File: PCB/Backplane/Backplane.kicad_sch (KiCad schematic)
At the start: 0 parts

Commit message: Backplane connectors
Got the labeling on the connectors done, just the connecting needs to be done
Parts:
- added J1, J10, J2, J3, J4, J5, J6, J7, J8, J9: 5530843-7, 5530843-7:TE_5530843-7, symbol 5530843-7:5530843-7
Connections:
- new net 1: J1.1, J10.1, J2.1, J3.1, J4.1, J5.1, J6.1, J7.1, J8.1, J9.1
- new net 10: J1.10, J10.10, J2.10, J3.10, J4.10, J5.10, J6.10, J7.10, J8.10, J9.10
- new net 11: J1.11, J10.11, J2.11, J3.11, J4.11, J5.11, J6.11, J7.11, J8.11, J9.11
- new net 12: J1.12, J10.12, J2.12, J3.12, J4.12, J5.12, J6.12, J7.12, J8.12, J9.12
- new net 13: J1.13, J10.13, J2.13, J3.13, J4.13, J5.13, J6.13, J7.13, J8.13, J9.13
- new net 14: J1.14, J10.14, J2.14, J3.14, J4.14, J5.14, J6.14, J7.14, J8.14, J9.14
- new net 15: J1.15, J10.15, J2.15, J3.15, J4.15, J5.15, J6.15, J7.15, J8.15, J9.15
- new net 16: J1.16, J10.16, J2.16, J3.16, J4.16, J5.16, J6.16, J7.16, J8.16, J9.16
- new net 17: J1.17, J10.17, J2.17, J3.17, J4.17, J5.17, J6.17, J7.17, J8.17, J9.17
- new net 18: J1.18, J10.18, J2.18, J3.18, J4.18, J5.18, J6.18, J7.18, J8.18, J9.18
- new net 19: J1.19, J10.19, J2.19, J3.19, J4.19, J5.19, J6.19, J7.19, J8.19, J9.19
- new net 2: J1.2, J10.2, J2.2, J3.2, J4.2, J5.2, J6.2, J7.2, J8.2, J9.2
- new net 20: J1.20, J10.20, J2.20, J3.20, J4.20, J5.20, J6.20, J7.20, J8.20, J9.20
- new net 21: J1.21, J10.21, J2.21, J3.21, J4.21, J5.21, J6.21, J7.21, J8.21, J9.21
- new net 22: J1.22, J10.22, J2.22, J3.22, J4.22, J5.22, J6.22, J7.22, J8.22, J9.22
- new net 23: J1.23, J10.23, J2.23, J3.23, J4.23, J5.23, J6.23, J7.23, J8.23, J9.23
- new net 24: J1.24, J10.24, J2.24, J3.24, J4.24, J5.24, J6.24, J7.24, J8.24, J9.24
- new net 25: J1.25, J10.25, J2.25, J3.25, J4.25, J5.25, J6.25, J7.25, J8.25, J9.25
- new net 26: J1.26, J10.26, J2.26, J3.26, J4.26, J5.26, J6.26, J7.26, J8.26, J9.26
- new net 27: J1.27, J10.27, J2.27, J3.27, J4.27, J5.27, J6.27, J7.27, J8.27, J9.27
- new net 28: J1.28, J10.28, J2.28, J3.28, J4.28, J5.28, J6.28, J7.28, J8.28, J9.28
- new net 29: J1.29, J10.29, J2.29, J3.29, J4.29, J5.29, J6.29, J7.29, J8.29, J9.29
- new net 3: J1.3, J10.3, J2.3, J3.3, J4.3, J5.3, J6.3, J7.3, J8.3, J9.3
- new net 30: J1.30, J10.30, J2.30, J3.30, J4.30, J5.30, J6.30, J7.30, J8.30, J9.30
- new net 31: J1.31, J10.31, J2.31, J3.31, J4.31, J5.31, J6.31, J7.31, J8.31, J9.31
- new net 32: J1.32, J10.32, J2.32, J3.32, J4.32, J5.32, J6.32, J7.32, J8.32, J9.32
- new net 33: J1.33, J10.33, J2.33, J3.33, J4.33, J5.33, J6.33, J7.33, J8.33, J9.33
- new net 34: J1.34, J10.34, J2.34, J3.34, J4.34, J5.34, J6.34, J7.34, J8.34, J9.34
- new net 35: J1.35, J10.35, J2.35, J3.35, J4.35, J5.35, J6.35, J7.35, J8.35, J9.35
- new net 36: J1.36, J10.36, J2.36, J3.36, J4.36, J5.36, J6.36, J7.36, J8.36, J9.36
- new net 37: J1.37, J10.37, J2.37, J3.37, J4.37, J5.37, J6.37, J7.37, J8.37, J9.37
- new net 38: J1.38, J10.38, J2.38, J3.38, J4.38, J5.38, J6.38, J7.38, J8.38, J9.38
- new net 39: J1.39, J10.39, J2.39, J3.39, J4.39, J5.39, J6.39, J7.39, J8.39, J9.39
- new net 4: J1.4, J10.4, J2.4, J3.4, J4.4, J5.4, J6.4, J7.4, J8.4, J9.4
- new net 40: J1.40, J10.40, J2.40, J3.40, J4.40, J5.40, J6.40, J7.40, J8.40, J9.40
- new net 41: J1.41, J10.41, J2.41, J3.41, J4.41, J5.41, J6.41, J7.41, J8.41, J9.41
- new net 42: J1.42, J10.42, J2.42, J3.42, J4.42, J5.42, J6.42, J7.42, J8.42, J9.42
- new net 43: J1.43, J10.43, J2.43, J3.43, J4.43, J5.43, J6.43, J7.43, J8.43, J9.43
- new net 44: J1.44, J10.44, J2.44, J3.44, J4.44, J5.44, J6.44, J7.44, J8.44, J9.44
- new net 45: J1.45, J10.45, J2.45, J3.45, J4.45, J5.45, J6.45, J7.45, J8.45, J9.45
- new net 46: J1.46, J10.46, J2.46, J3.46, J4.46, J5.46, J6.46, J7.46, J8.46, J9.46
- new net 47: J1.47, J10.47, J2.47, J3.47, J4.47, J5.47, J6.47, J7.47, J8.47, J9.47
- new net 48: J1.48, J10.48, J2.48, J3.48, J4.48, J5.48, J6.48, J7.48, J8.48, J9.48
- new net 49: J1.49, J10.49, J2.49, J3.49, J4.49, J5.49, J6.49, J7.49, J8.49, J9.49
- new net 5: J1.5, J10.5, J2.5, J3.5, J4.5, J5.5, J6.5, J7.5, J8.5, J9.5
- new net 50: J1.50, J10.50, J2.50, J3.50, J4.50, J5.50, J6.50, J7.50, J8.50, J9.50
- new net 51: J1.51, J10.51, J2.51, J3.51, J4.51, J5.51, J6.51, J7.51, J8.51, J9.51
- new net 52: J1.52, J10.52, J2.52, J3.52, J4.52, J5.52, J6.52, J7.52, J8.52, J9.52
- new net 53: J1.53, J10.53, J2.53, J3.53, J4.53, J5.53, J6.53, J7.53, J8.53, J9.53
- new net 54: J1.54, J10.54, J2.54, J3.54, J4.54, J5.54, J6.54, J7.54, J8.54, J9.54
- new net 55: J1.55, J10.55, J2.55, J3.55, J4.55, J5.55, J6.55, J7.55, J8.55, J9.55
- new net 56: J1.56, J10.56, J2.56, J3.56, J4.56, J5.56, J6.56, J7.56, J8.56, J9.56
- new net 57: J1.57, J10.57, J2.57, J3.57, J4.57, J5.57, J6.57, J7.57, J8.57, J9.57
- new net 58: J1.58, J10.58, J2.58, J3.58, J4.58, J5.58, J6.58, J7.58, J8.58, J9.58
- new net 59: J1.59, J10.59, J2.59, J3.59, J4.59, J5.59, J6.59, J7.59, J8.59, J9.59
- new net 6: J1.6, J10.6, J2.6, J3.6, J4.6, J5.6, J6.6, J7.6, J8.6, J9.6
- new net 60: J1.60, J10.60, J2.60, J3.60, J4.60, J5.60, J6.60, J7.60, J8.60, J9.60
- new net 7: J1.7, J10.7, J2.7, J3.7, J4.7, J5.7, J6.7, J7.7, J8.7, J9.7
- new net 8: J1.8, J10.8, J2.8, J3.8, J4.8, J5.8, J6.8, J7.8, J8.8, J9.8
- new net 9: J1.9, J10.9, J2.9, J3.9, J4.9, J5.9, J6.9, J7.9, J8.9, J9.9

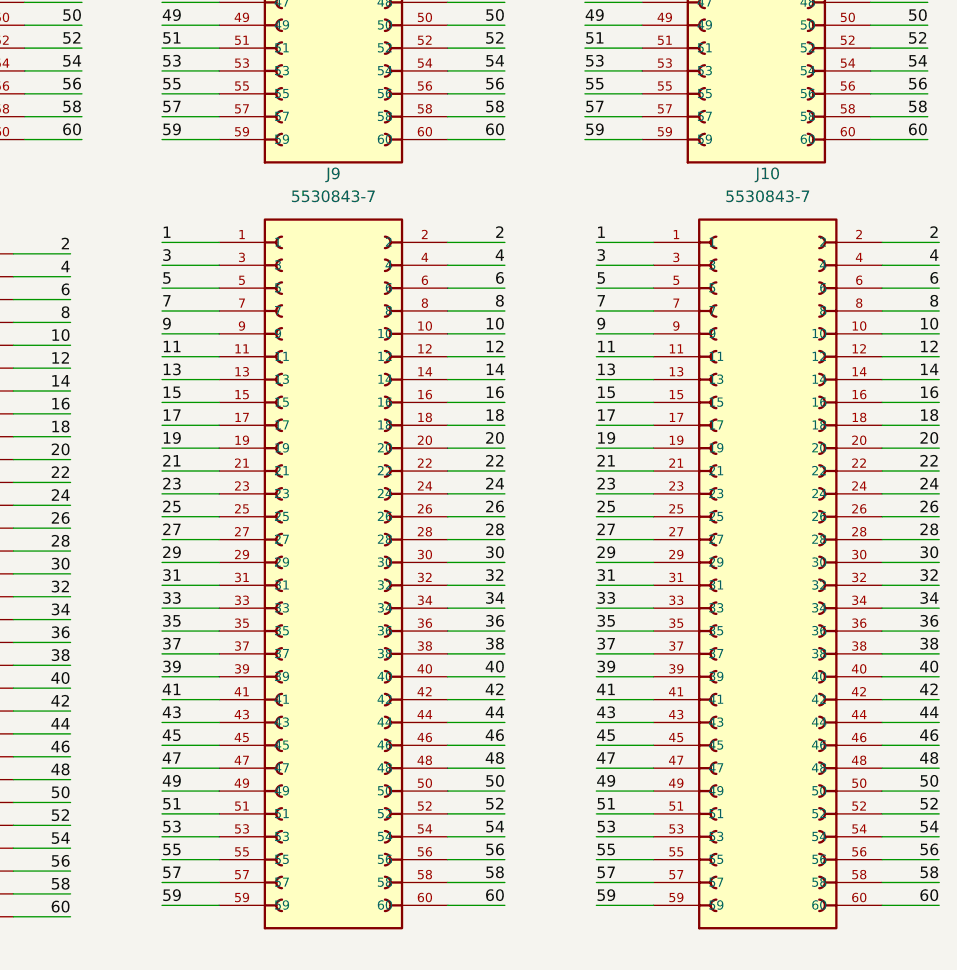
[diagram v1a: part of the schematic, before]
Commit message: Updated backplane and removed unused connectors
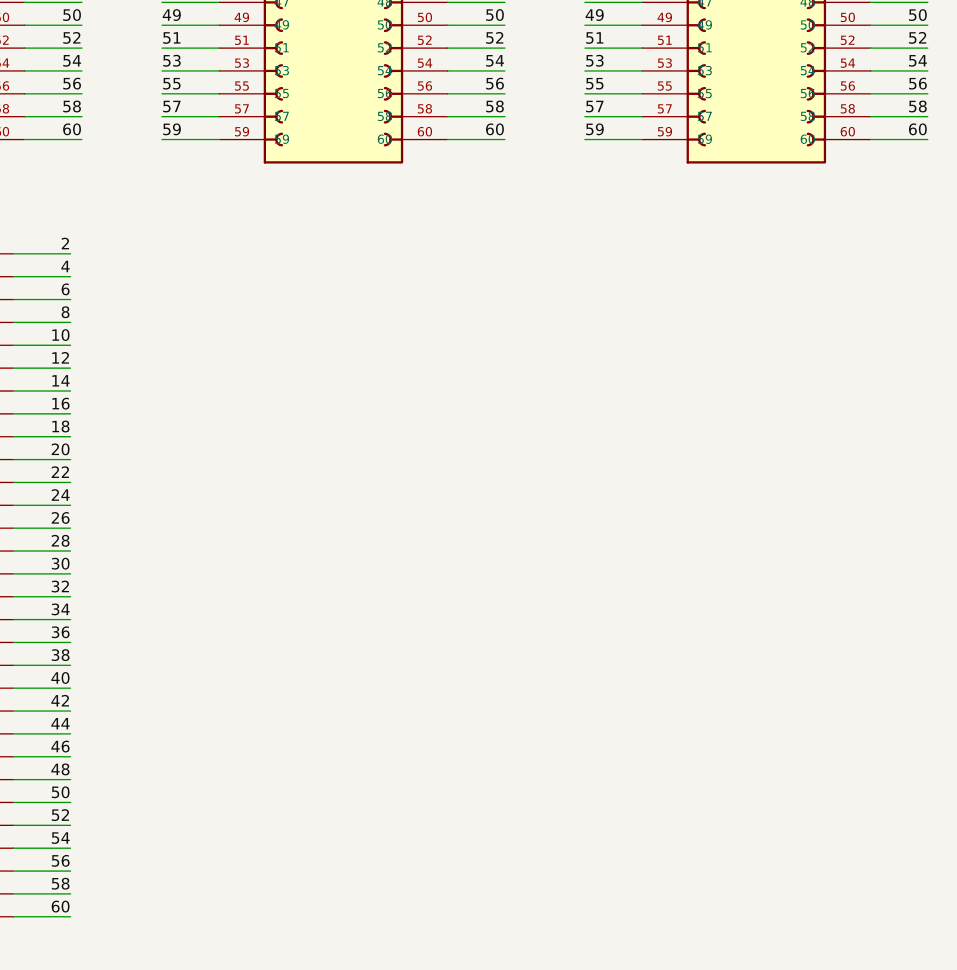
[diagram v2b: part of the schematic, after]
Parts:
- removed J10, J9: 5530843-7, 5530843-7:TE_5530843-7, symbol 5530843-7:5530843-7

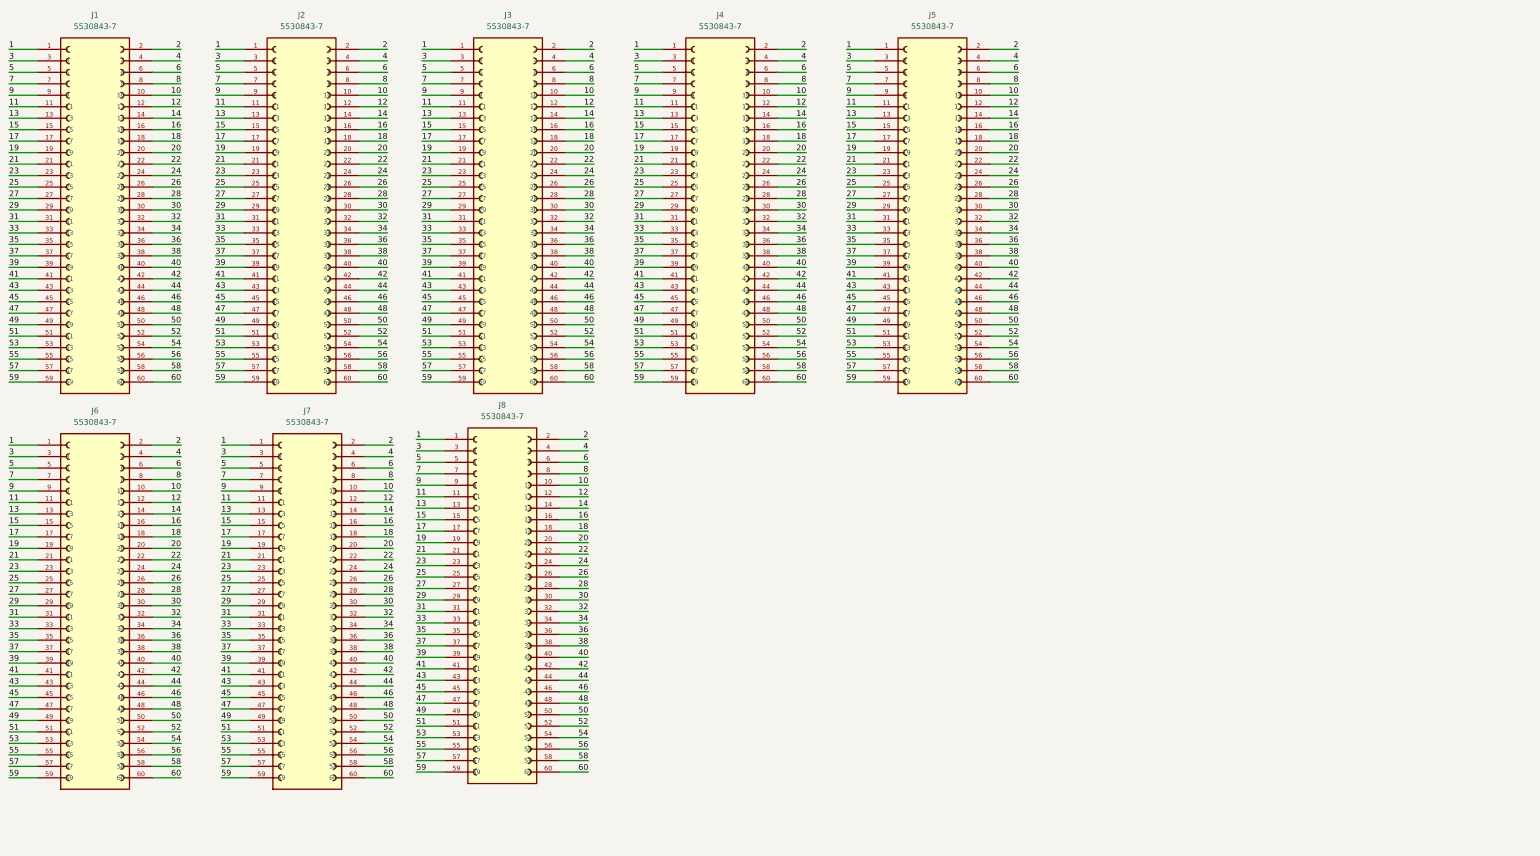
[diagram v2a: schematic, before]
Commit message: Finished new backplane
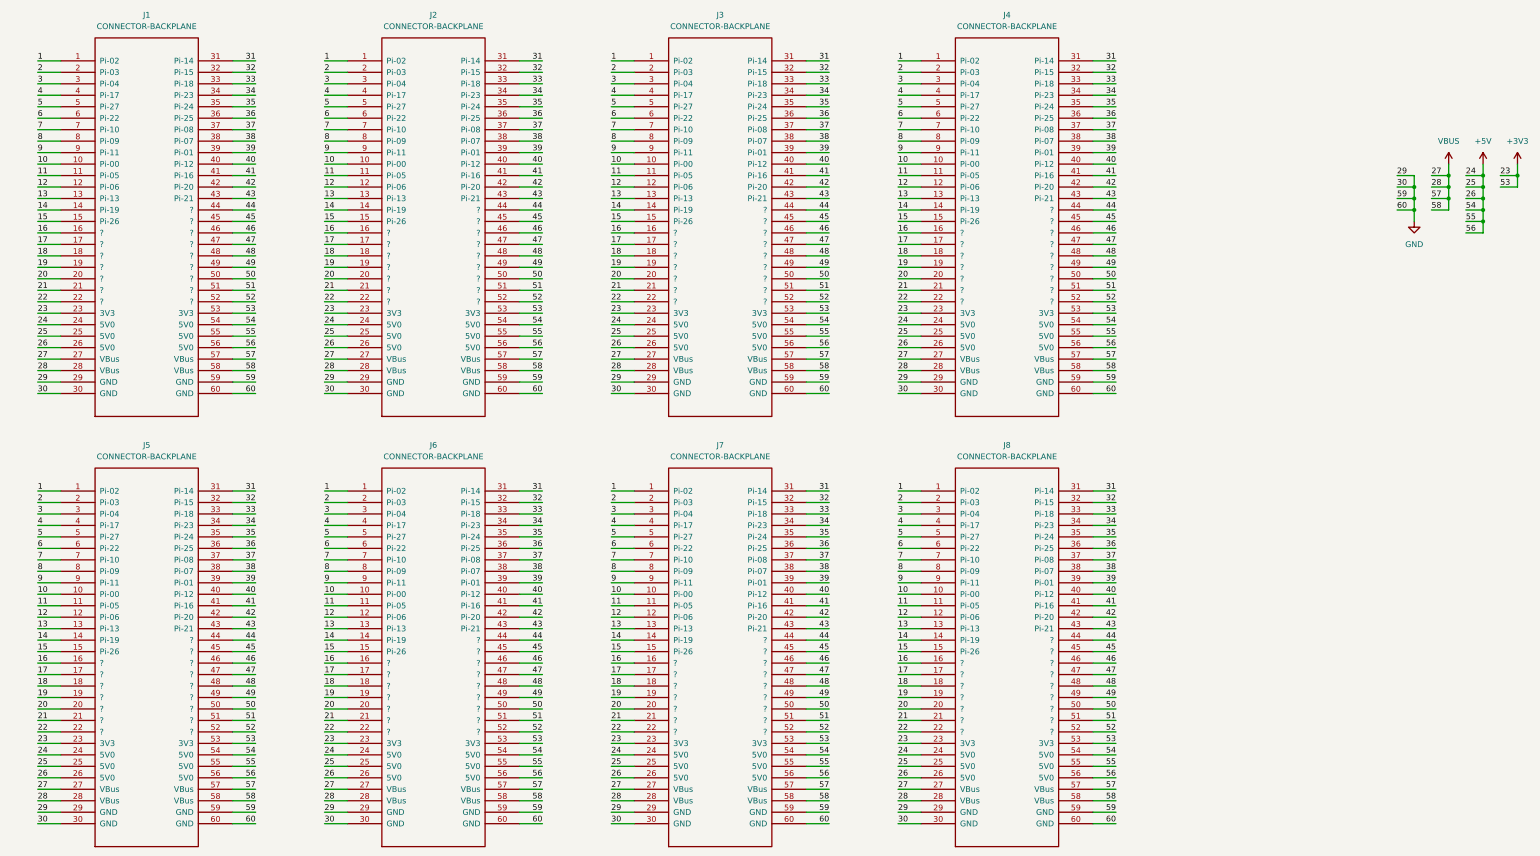
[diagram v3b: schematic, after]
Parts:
- removed J1, J2, J3, J4, J5, J6, J7, J8: 5530843-7, 5530843-7:TE_5530843-7, symbol 5530843-7:5530843-7
- added J1, J2, J3, J4, J5, J6, J7, J8: CONNECTOR-BACKPLANE, 5530843-7:TE_5530843-7, symbol 5530843-7:CONNECTOR-BACKPLANE
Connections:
- net 1: now also J1.1 (Pi-02), J2.1 (Pi-02), J3.1 (Pi-02), J4.1 (Pi-02), J5.1 (Pi-02), J6.1 (Pi-02), J7.1 (Pi-02), J8.1 (Pi-02)
- net 10: now also J1.10 (Pi-00), J2.10 (Pi-00), J3.10 (Pi-00), J4.10 (Pi-00), J5.10 (Pi-00), J6.10 (Pi-00), J7.10 (Pi-00), J8.10 (Pi-00)
- net 11: now also J1.11 (Pi-05), J2.11 (Pi-05), J3.11 (Pi-05), J4.11 (Pi-05), J5.11 (Pi-05), J6.11 (Pi-05), J7.11 (Pi-05), J8.11 (Pi-05)
- net 12: now also J1.12 (Pi-06), J2.12 (Pi-06), J3.12 (Pi-06), J4.12 (Pi-06), J5.12 (Pi-06), J6.12 (Pi-06), J7.12 (Pi-06), J8.12 (Pi-06)
- net 13: now also J1.13 (Pi-13), J2.13 (Pi-13), J3.13 (Pi-13), J4.13 (Pi-13), J5.13 (Pi-13), J6.13 (Pi-13), J7.13 (Pi-13), J8.13 (Pi-13)
- net 14: now also J1.14 (Pi-19), J2.14 (Pi-19), J3.14 (Pi-19), J4.14 (Pi-19), J5.14 (Pi-19), J6.14 (Pi-19), J7.14 (Pi-19), J8.14 (Pi-19)
- net 15: now also J1.15 (Pi-26), J2.15 (Pi-26), J3.15 (Pi-26), J4.15 (Pi-26), J5.15 (Pi-26), J6.15 (Pi-26), J7.15 (Pi-26), J8.15 (Pi-26)
- net 16: now also J1.16 (?), J2.16 (?), J3.16 (?), J4.16 (?), J5.16 (?), J6.16 (?), J7.16 (?), J8.16 (?)
- net 17: now also J1.17 (?), J2.17 (?), J3.17 (?), J4.17 (?), J5.17 (?), J6.17 (?), J7.17 (?), J8.17 (?)
- net 18: now also J1.18 (?), J2.18 (?), J3.18 (?), J4.18 (?), J5.18 (?), J6.18 (?), J7.18 (?), J8.18 (?)
- net 19: now also J1.19 (?), J2.19 (?), J3.19 (?), J4.19 (?), J5.19 (?), J6.19 (?), J7.19 (?), J8.19 (?)
- net 2: now also J1.2 (Pi-03), J2.2 (Pi-03), J3.2 (Pi-03), J4.2 (Pi-03), J5.2 (Pi-03), J6.2 (Pi-03), J7.2 (Pi-03), J8.2 (Pi-03)
- net 20: now also J1.20 (?), J2.20 (?), J3.20 (?), J4.20 (?), J5.20 (?), J6.20 (?), J7.20 (?), J8.20 (?)
- net 21: now also J1.21 (?), J2.21 (?), J3.21 (?), J4.21 (?), J5.21 (?), J6.21 (?), J7.21 (?), J8.21 (?)
- net 22: now also J1.22 (?), J2.22 (?), J3.22 (?), J4.22 (?), J5.22 (?), J6.22 (?), J7.22 (?), J8.22 (?)
- net 3: now also J1.3 (Pi-04), J2.3 (Pi-04), J3.3 (Pi-04), J4.3 (Pi-04), J5.3 (Pi-04), J6.3 (Pi-04), J7.3 (Pi-04), J8.3 (Pi-04)
- net 31: now also J1.31 (Pi-14), J2.31 (Pi-14), J3.31 (Pi-14), J4.31 (Pi-14), J5.31 (Pi-14), J6.31 (Pi-14), J7.31 (Pi-14), J8.31 (Pi-14)
- net 32: now also J1.32 (Pi-15), J2.32 (Pi-15), J3.32 (Pi-15), J4.32 (Pi-15), J5.32 (Pi-15), J6.32 (Pi-15), J7.32 (Pi-15), J8.32 (Pi-15)
- net 33: now also J1.33 (Pi-18), J2.33 (Pi-18), J3.33 (Pi-18), J4.33 (Pi-18), J5.33 (Pi-18), J6.33 (Pi-18), J7.33 (Pi-18), J8.33 (Pi-18)
- net 34: now also J1.34 (Pi-23), J2.34 (Pi-23), J3.34 (Pi-23), J4.34 (Pi-23), J5.34 (Pi-23), J6.34 (Pi-23), J7.34 (Pi-23), J8.34 (Pi-23)
- net 35: now also J1.35 (Pi-24), J2.35 (Pi-24), J3.35 (Pi-24), J4.35 (Pi-24), J5.35 (Pi-24), J6.35 (Pi-24), J7.35 (Pi-24), J8.35 (Pi-24)
- net 36: now also J1.36 (Pi-25), J2.36 (Pi-25), J3.36 (Pi-25), J4.36 (Pi-25), J5.36 (Pi-25), J6.36 (Pi-25), J7.36 (Pi-25), J8.36 (Pi-25)
- net 37: now also J1.37 (Pi-08), J2.37 (Pi-08), J3.37 (Pi-08), J4.37 (Pi-08), J5.37 (Pi-08), J6.37 (Pi-08), J7.37 (Pi-08), J8.37 (Pi-08)
- net 38: now also J1.38 (Pi-07), J2.38 (Pi-07), J3.38 (Pi-07), J4.38 (Pi-07), J5.38 (Pi-07), J6.38 (Pi-07), J7.38 (Pi-07), J8.38 (Pi-07)
- net 39: now also J1.39 (Pi-01), J2.39 (Pi-01), J3.39 (Pi-01), J4.39 (Pi-01), J5.39 (Pi-01), J6.39 (Pi-01), J7.39 (Pi-01), J8.39 (Pi-01)
- net 4: now also J1.4 (Pi-17), J2.4 (Pi-17), J3.4 (Pi-17), J4.4 (Pi-17), J5.4 (Pi-17), J6.4 (Pi-17), J7.4 (Pi-17), J8.4 (Pi-17)
- net 40: now also J1.40 (Pi-12), J2.40 (Pi-12), J3.40 (Pi-12), J4.40 (Pi-12), J5.40 (Pi-12), J6.40 (Pi-12), J7.40 (Pi-12), J8.40 (Pi-12)
- net 41: now also J1.41 (Pi-16), J2.41 (Pi-16), J3.41 (Pi-16), J4.41 (Pi-16), J5.41 (Pi-16), J6.41 (Pi-16), J7.41 (Pi-16), J8.41 (Pi-16)
- net 42: now also J1.42 (Pi-20), J2.42 (Pi-20), J3.42 (Pi-20), J4.42 (Pi-20), J5.42 (Pi-20), J6.42 (Pi-20), J7.42 (Pi-20), J8.42 (Pi-20)
- net 43: now also J1.43 (Pi-21), J2.43 (Pi-21), J3.43 (Pi-21), J4.43 (Pi-21), J5.43 (Pi-21), J6.43 (Pi-21), J7.43 (Pi-21), J8.43 (Pi-21)
- net 44: now also J1.44 (?), J2.44 (?), J3.44 (?), J4.44 (?), J5.44 (?), J6.44 (?), J7.44 (?), J8.44 (?)
- net 45: now also J1.45 (?), J2.45 (?), J3.45 (?), J4.45 (?), J5.45 (?), J6.45 (?), J7.45 (?), J8.45 (?)
- net 46: now also J1.46 (?), J2.46 (?), J3.46 (?), J4.46 (?), J5.46 (?), J6.46 (?), J7.46 (?), J8.46 (?)
- net 47: now also J1.47 (?), J2.47 (?), J3.47 (?), J4.47 (?), J5.47 (?), J6.47 (?), J7.47 (?), J8.47 (?)
- net 48: now also J1.48 (?), J2.48 (?), J3.48 (?), J4.48 (?), J5.48 (?), J6.48 (?), J7.48 (?), J8.48 (?)
- net 49: now also J1.49 (?), J2.49 (?), J3.49 (?), J4.49 (?), J5.49 (?), J6.49 (?), J7.49 (?), J8.49 (?)
- net 5: now also J1.5 (Pi-27), J2.5 (Pi-27), J3.5 (Pi-27), J4.5 (Pi-27), J5.5 (Pi-27), J6.5 (Pi-27), J7.5 (Pi-27), J8.5 (Pi-27)
- net 50: now also J1.50 (?), J2.50 (?), J3.50 (?), J4.50 (?), J5.50 (?), J6.50 (?), J7.50 (?), J8.50 (?)
- net 51: now also J1.51 (?), J2.51 (?), J3.51 (?), J4.51 (?), J5.51 (?), J6.51 (?), J7.51 (?), J8.51 (?)
- net 52: now also J1.52 (?), J2.52 (?), J3.52 (?), J4.52 (?), J5.52 (?), J6.52 (?), J7.52 (?), J8.52 (?)
- net 6: now also J1.6 (Pi-22), J2.6 (Pi-22), J3.6 (Pi-22), J4.6 (Pi-22), J5.6 (Pi-22), J6.6 (Pi-22), J7.6 (Pi-22), J8.6 (Pi-22)
- net 7: now also J1.7 (Pi-10), J2.7 (Pi-10), J3.7 (Pi-10), J4.7 (Pi-10), J5.7 (Pi-10), J6.7 (Pi-10), J7.7 (Pi-10), J8.7 (Pi-10)
- net 8: now also J1.8 (Pi-09), J2.8 (Pi-09), J3.8 (Pi-09), J4.8 (Pi-09), J5.8 (Pi-09), J6.8 (Pi-09), J7.8 (Pi-09), J8.8 (Pi-09)
- net 9: now also J1.9 (Pi-11), J2.9 (Pi-11), J3.9 (Pi-11), J4.9 (Pi-11), J5.9 (Pi-11), J6.9 (Pi-11), J7.9 (Pi-11), J8.9 (Pi-11)
- new net +3V3: J1.23 (3V3), J1.53 (3V3), J2.23 (3V3), J2.53 (3V3), J3.23 (3V3), J3.53 (3V3), J4.23 (3V3), J4.53 (3V3), J5.23 (3V3), J5.53 (3V3), J6.23 (3V3), J6.53 (3V3), J7.23 (3V3), J7.53 (3V3), J8.23 (3V3), J8.53 (3V3)
- new net +5V: J1.24 (5V0), J1.25 (5V0), J1.26 (5V0), J1.54 (5V0), J1.55 (5V0), J1.56 (5V0), J2.24 (5V0), J2.25 (5V0), J2.26 (5V0), J2.54 (5V0), J2.55 (5V0), J2.56 (5V0), J3.24 (5V0), J3.25 (5V0), J3.26 (5V0), J3.54 (5V0), J3.55 (5V0), J3.56 (5V0), J4.24 (5V0), J4.25 (5V0), J4.26 (5V0), J4.54 (5V0), J4.55 (5V0), J4.56 (5V0), J5.24 (5V0), J5.25 (5V0), J5.26 (5V0), J5.54 (5V0), J5.55 (5V0), J5.56 (5V0), J6.24 (5V0), J6.25 (5V0), J6.26 (5V0), J6.54 (5V0), J6.55 (5V0), J6.56 (5V0), J7.24 (5V0), J7.25 (5V0), J7.26 (5V0), J7.54 (5V0), J7.55 (5V0), J7.56 (5V0), J8.24 (5V0), J8.25 (5V0), J8.26 (5V0), J8.54 (5V0), J8.55 (5V0), J8.56 (5V0)
- new net GND: J1.29 (GND), J1.30 (GND), J1.59 (GND), J1.60 (GND), J2.29 (GND), J2.30 (GND), J2.59 (GND), J2.60 (GND), J3.29 (GND), J3.30 (GND), J3.59 (GND), J3.60 (GND), J4.29 (GND), J4.30 (GND), J4.59 (GND), J4.60 (GND), J5.29 (GND), J5.30 (GND), J5.59 (GND), J5.60 (GND), J6.29 (GND), J6.30 (GND), J6.59 (GND), J6.60 (GND), J7.29 (GND), J7.30 (GND), J7.59 (GND), J7.60 (GND), J8.29 (GND), J8.30 (GND), J8.59 (GND), J8.60 (GND)
- new net VBUS: J1.27 (VBus), J1.28 (VBus), J1.57 (VBus), J1.58 (VBus), J2.27 (VBus), J2.28 (VBus), J2.57 (VBus), J2.58 (VBus), J3.27 (VBus), J3.28 (VBus), J3.57 (VBus), J3.58 (VBus), J4.27 (VBus), J4.28 (VBus), J4.57 (VBus), J4.58 (VBus), J5.27 (VBus), J5.28 (VBus), J5.57 (VBus), J5.58 (VBus), J6.27 (VBus), J6.28 (VBus), J6.57 (VBus), J6.58 (VBus), J7.27 (VBus), J7.28 (VBus), J7.57 (VBus), J7.58 (VBus), J8.27 (VBus), J8.28 (VBus), J8.57 (VBus), J8.58 (VBus)
